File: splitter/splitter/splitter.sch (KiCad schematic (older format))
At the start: 26 parts, among them J1 JACKIN, J2 JACKSEND, J3 JACKRCV, J4 JACKOUT, J5 Barrel_Jack, SW1 SW_HIGHLOW, SW2 SW_POWER, SW3 SW_3PDT_x3, U1 TL074, U2 TLE2426xLP

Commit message: do pcb
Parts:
- removed J5: Barrel_Jack, symbol Connector:Barrel_Jack
- added J5: Jack-DC, Connector_PinSocket_2.54mm:PinSocket_1x02_P2.54mm_Vertical, symbol Connector:Jack-DC
- C1, C2: footprint (none) -> Capacitor_THT:C_Disc_D4.3mm_W1.9mm_P5.00mm
- C3, C4: renamed from C?; footprint (none) -> Capacitor_THT:CP_Radial_D6.3mm_P2.50mm
- D1: renamed from D?; footprint (none) -> LED_THT:LED_D3.0mm
- J1, J2, J3, J4: footprint (none) -> Connector_Audio:Jack_6.35mm_Neutrik_NMJ6HCD2_Horizontal
- R1, R2, R3, R4, R5, R6, R7, R8: footprint (none) -> Resistor_THT:R_Axial_DIN0207_L6.3mm_D2.5mm_P7.62mm_Horizontal
- R9: renamed from R?; footprint (none) -> Resistor_THT:R_Axial_DIN0207_L6.3mm_D2.5mm_P7.62mm_Horizontal
- RV1, RV2: footprint (none) -> Potentiometer_THT:Potentiometer_Alpha_RD902F-40-00D_Dual_Vertical
- SW1: footprint (none) -> Button_Switch_THT:MTS-200_DPDT_6T
- SW2: renamed from SW3; value SW_3PDT_x3 -> SW_POWER; footprint (none) -> Connector_PinSocket_2.54mm:PinSocket_3x03_P2.54mm_Vertical
- SW2: footprint (none) -> Connector_PinSocket_2.54mm:PinSocket_3x03_P2.54mm_Vertical
- U1: footprint (none) -> Package_DIP:DIP-14_W7.62mm
- U2: footprint (none) -> Package_TO_SOT_THT:TO-92_Inline
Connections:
- net GND: now also U2.1 (OUT); no longer U2.2 (COMMON)
- net HIGH: now also U1.1, U1.2 (-); no longer U1.6 (-), U1.7
- net IN: now also U1.5 (+); no longer U1.3 (+)
- net at C2.1, R2.2: now also U1.3 (+); no longer U1.5 (+)
- net at SW2.2 (B): now also J5.1
- net VCC renamed +9V
- net VDD renamed GNDD
- net GNDD: now also U2.2 (COMMON), J5.2; no longer U2.1 (OUT)
- new net: C1.2, U1.6 (-), U1.7
- no-connect marks 2 -> 3
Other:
- note added: "Ground case to GNDD"
- note removed: "Ground case to VDD"
- moved on the sheet: U1A, U1B

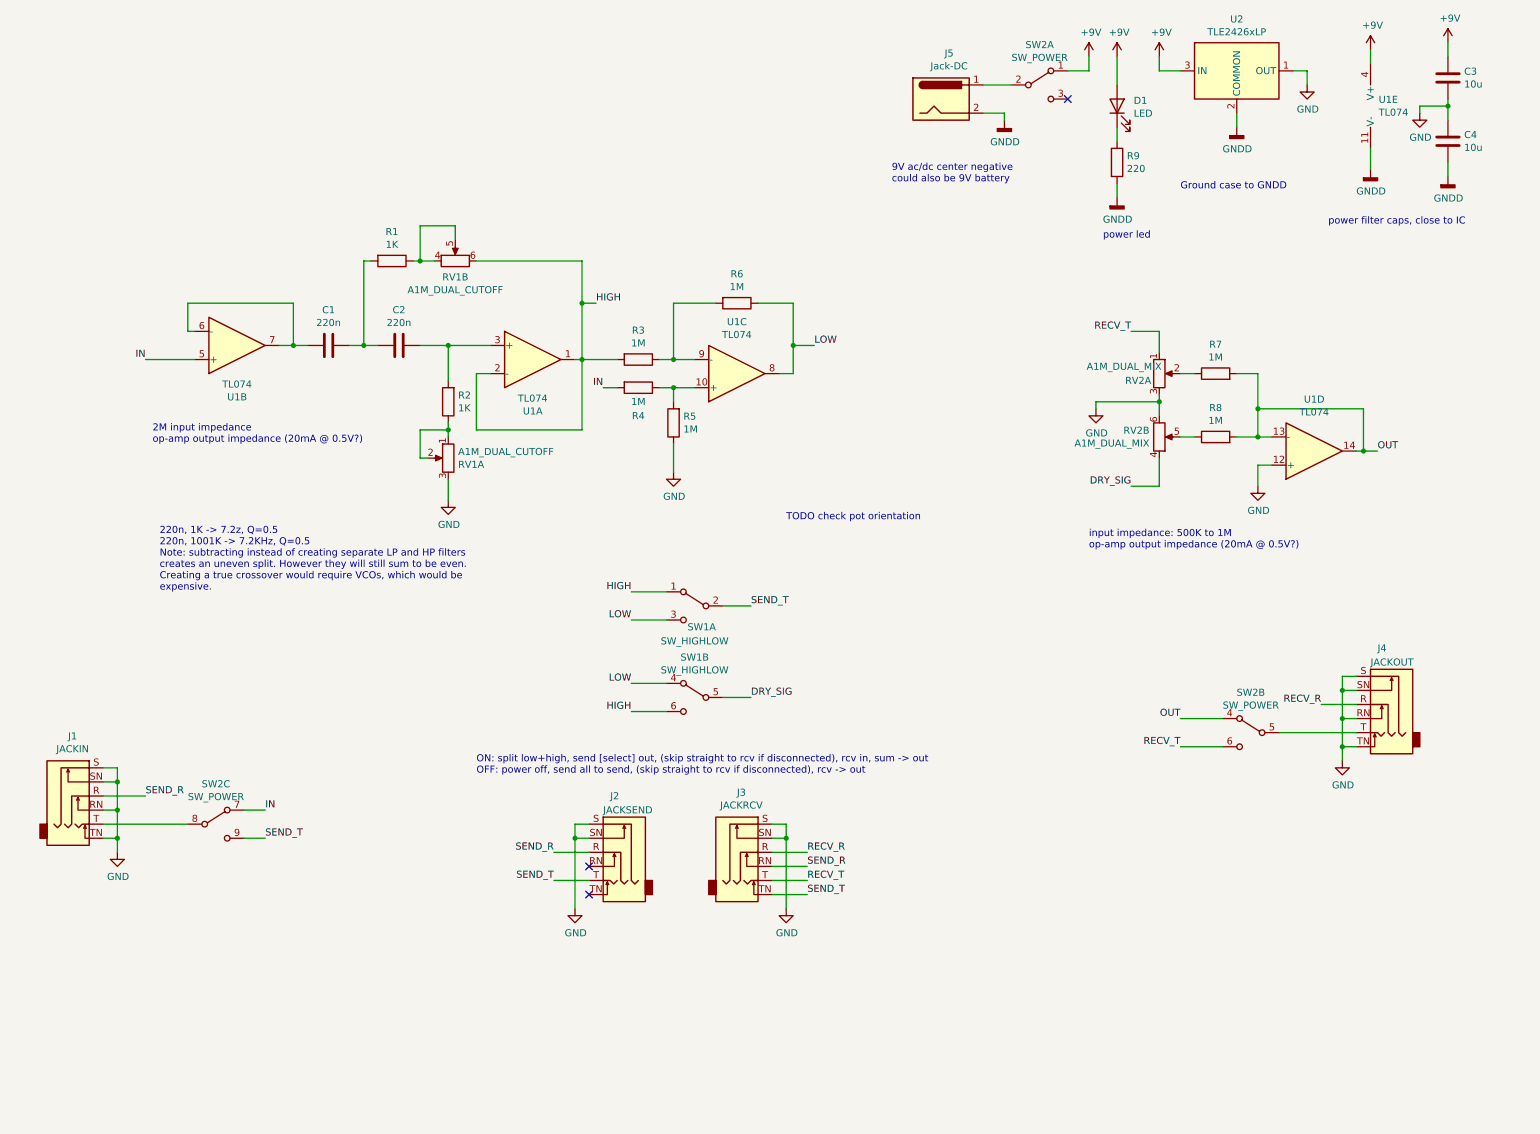
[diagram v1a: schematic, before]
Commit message: rework switches to allow low/high/all send and bypass
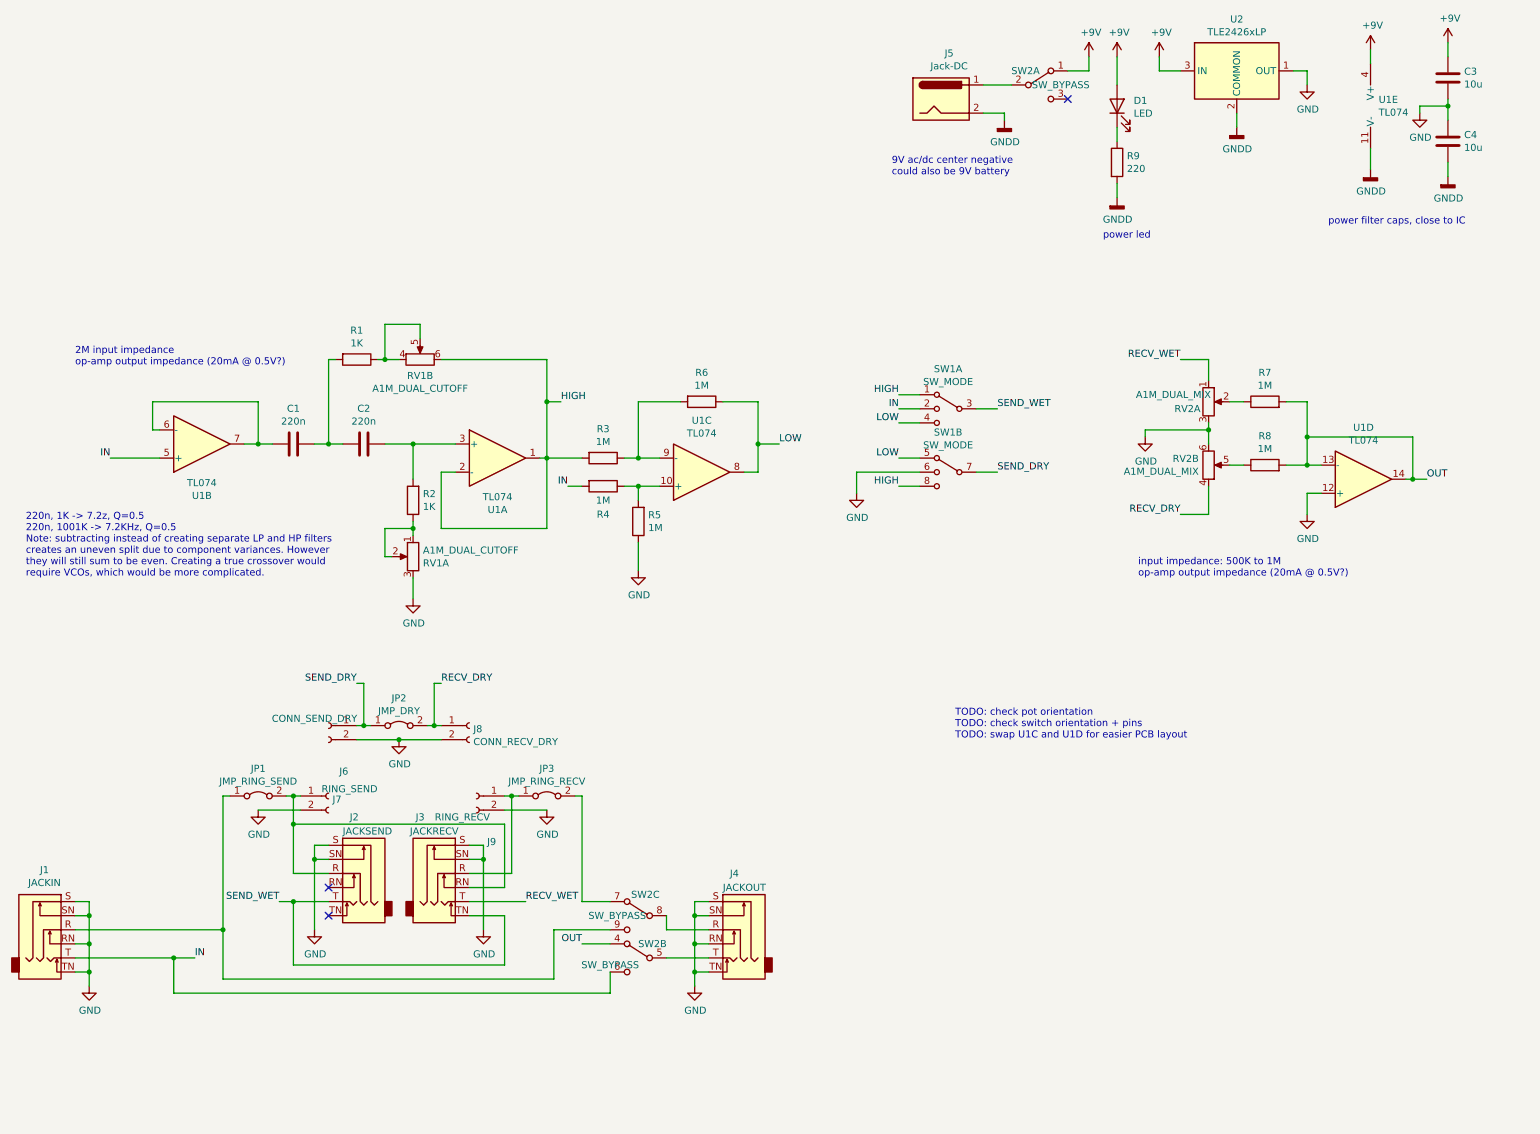
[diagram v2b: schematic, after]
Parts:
- removed SW1: SW_HIGHLOW, Button_Switch_THT:MTS-200_DPDT_6T, symbol Switch:SW_DPDT_x2
- added J6: CONN_SEND_DRY, Connector_PinSocket_2.54mm:PinSocket_1x02_P2.54mm_Vertical, symbol Connector:Conn_01x02_Female
- added J7: RING_SEND, Connector_PinSocket_2.54mm:PinSocket_1x02_P2.54mm_Vertical, symbol Connector:Conn_01x02_Female
- added J8: CONN_RECV_DRY, Connector_PinSocket_2.54mm:PinSocket_1x02_P2.54mm_Vertical, symbol Connector:Conn_01x02_Female
- added J9: RING_RECV, Connector_PinSocket_2.54mm:PinSocket_1x02_P2.54mm_Vertical, symbol Connector:Conn_01x02_Female
- added JP1: JMP_RING_SEND, Jumper:SolderJumper-2_P1.3mm_Open_RoundedPad1.0x1.5mm, symbol Jumper:Jumper_2_Bridged
- added JP2: JMP_DRY, Jumper:SolderJumper-2_P1.3mm_Open_RoundedPad1.0x1.5mm, symbol Jumper:Jumper_2_Bridged
- added JP3: JMP_RING_RECV, Jumper:SolderJumper-2_P1.3mm_Open_RoundedPad1.0x1.5mm, symbol Jumper:Jumper_2_Bridged
- added SW1: SW_MODE, Button_Switch_THT:SW_EG2301_DP3T, symbol Switch:SW_DP3T
- J3: value JACKRCV -> JACKRECV
- SW2: value SW_POWER -> SW_BYPASS
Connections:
- net GND: now also J6.2 (Pin_2), J7.2 (Pin_2), J8.2 (Pin_2), J9.2 (Pin_2), SW1.6
- net HIGH: now also SW1.1, SW1.8
- net IN: now also J1.T, SW2.6 (C), SW1.2; no longer SW2.7 (A)
- net LOW: now also SW1.4, SW1.5
- net at SW2.8 (B): now also J4.R; no longer J1.T
- net DRY_SIG renamed RECV_DRY
- net RECV_DRY: now also J8.1 (Pin_1), JP2.2 (B)
- net RECV_R: no longer names the net of J3.R
- net RECV_R: now also J9.1 (Pin_1), JP3.1 (A); no longer J4.R
- net RECV_T renamed RECV_WET
- net RECV_WET: no longer SW2.6 (C)
- net SEND_R: no longer names the net of J2.R, J3.RN
- net SEND_R: now also J7.1 (Pin_1), JP1.2 (B); no longer J1.R
- net SEND_T renamed SEND_WET
- net SEND_WET: now also SW1.3; no longer SW2.9 (C)
- new net: JP3.2 (B), SW2.7 (A)
- new net: J1.R, JP1.1 (A), SW2.9 (C)
- new net SEND_DRY: J6.1 (Pin_1), JP2.1 (A), SW1.7
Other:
- note added: "220n, 1K -> 7.2z, Q=0.5\n220n, 1001K -> 7.2KHz, Q=0.5\nNote: subtracting instead of creating separate LP and HP filters\ncreates an uneven split due to component variances. However\nthey will still sum to be even. Creating a true crossover would\nrequire VCOs, which would be more complicated."
- note added: "TODO: check pot orientation\nTODO: check switch orientation + pins\nTODO: swap U1C and U1D for easier PCB layout"
- note removed: "220n, 1K -> 7.2z, Q=0.5\n220n, 1001K -> 7.2KHz, Q=0.5\nNote: subtracting instead of creating separate LP and HP filters\ncreates an uneven split. However they will still sum to be even.\nCreating a true crossover would require VCOs, which would be\nexpensive."
- note removed: "Ground case to GNDD"
- note removed: "ON: split low+high, send [select] out, (skip straight to rcv if disconnected), rcv in, sum -> out\nOFF: power off, send all to send, (skip straight to rcv if disconnected), rcv -> out"
- note removed: "TODO check pot orientation"
- moved on the sheet: C1, C2, J1, J2, J3, J4, R1, R2, R3, R4, R5, R6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

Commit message: fix some bugs
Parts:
- added R10: 1M, Resistor_THT:R_Axial_DIN0207_L6.3mm_D2.5mm_P7.62mm_Horizontal, symbol Device:R
- C1, C2: value 220n -> 22n
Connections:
- net GND: now also RV2.1, U1.10 (+); no longer RV2.3, U1.12 (+)
- net LOW: now also U1.14; no longer U1.8
- net OUT: now also U1.8, R10.2; no longer R7.2, R8.2, U1.13 (-), U1.14
- net RECV_DRY: now also RV2.3; no longer RV2.4
- net RECV_WET: now also RV2.4; no longer RV2.1
- net at R4.1, R5.2: now also U1.12 (+); no longer U1.10 (+)
- net at R3.1, R6.2: now also U1.13 (-); no longer U1.9 (-)
- net at R8.1: now also RV2.2; no longer RV2.5
- net at R7.1: now also RV2.5; no longer RV2.2
- new net: R10.1, R7.2, R8.2, U1.9 (-)
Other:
- note added: "22n, 1K -> 7.2z, Q=0.5\n22n, 1001K -> 7.2KHz, Q=0.5\nNote: subtracting instead of creating separate LP and HP\nfilters creates an uneven split as opposed to summing LR\nfilters. Creating a true crossover would require VCOs,\nwhich would be more complicated."
- note added: "TODO: check pot orientation\nTODO: check switch orientation + pins\nTODO: verify mixer on bb\nTODO: verify switching on bb"
- note removed: "220n, 1K -> 7.2z, Q=0.5\n220n, 1001K -> 7.2KHz, Q=0.5\nNote: subtracting instead of creating separate LP and HP filters\ncreates an uneven split due to component variances. However\nthey will still sum to be even. Creating a true crossover would\nrequire VCOs, which would be more complicated."
- note removed: "TODO: check pot orientation\nTODO: check switch orientation + pins\nTODO: swap U1C and U1D for easier PCB layout"
- moved on the sheet: RV2A, RV2B, U1C, U1D
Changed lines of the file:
@@
 P 2700 3600
 F 0 "C1" V 2448 3600 50  0000 C CNN
-F 1 "220n" V 2539 3600 50  0000 C CNN
+F 1 "22n" V 2539 3600 50  0000 C CNN
 F 2 "Capacitor_THT:C_Disc_D4.3mm_W1.9mm_P5.00mm" H 2738 3450 50  0001 C CNN
 F 3 "~" H 2700 3600 50  0001 C CNN
@@
 P 3200 3600
 F 0 "C2" V 2948 3600 50  0000 C CNN
-F 1 "220n" V 3039 3600 50  0000 C CNN
+F 1 "22n" V 3039 3600 50  0000 C CNN
 F 2 "Capacitor_THT:C_Disc_D4.3mm_W1.9mm_P5.00mm" H 3238 3450 50  0001 C CNN
 F 3 "~" H 3200 3600 50  0001 C CNN
@@
 $EndComp
 Text Notes 800  4550 0    50   ~ 0
-220n, 1K -> 7.2z, Q=0.5\n220n, 1001K -> 7.2KHz, Q=0.5\nNote: subtracting instead of creating separate LP and HP filters\ncreates an uneven split due to component variances. However\nthey will still sum to be even. Creating a true crossover would\nrequire VCOs, which would be more complicated.
+22n, 1K -> 7.2z, Q=0.5\n22n, 1001K -> 7.2KHz, Q=0.5\nNote: subtracting instead of creating separate LP and HP\nfilters creates an uneven split as opposed to summing LR\nfilters. Creating a true crossover would require VCOs,\nwhich would be more complicated.
 $Comp
 L Amplifier_Operational:TL074 U1
@@
 $EndComp
 Text Notes 7400 5700 0    50   ~ 0
-TODO: check pot orientation\nTODO: check switch orientation + pins\nTODO: swap U1C and U1D for easier PCB layout
+TODO: check pot orientation\nTODO: check switch orientation + pins\nTODO: verify mixer on bb\nTODO: verify switching on bb
 $Comp
 L power:GND #PWR02
@@
 L Amplifier_Operational:TL074 U1
 U 3 1 62D6659B
-P 5600 3800
-F 0 "U1" H 5600 3433 50  0000 C CNN
-F 1 "TL074" H 5600 3524 50  0000 C CNN
-F 2 "Package_DIP:DIP-14_W7.62mm" H 5550 3900 50  0001 C CNN
-F 3 "http://www.ti.com/lit/ds/symlink/tl071.pdf" H 5650 4000 50  0001 C CNN
-	3    5600 3800
+P 10300 3850
+F 0 "U1" H 10300 3483 50  0000 C CNN
+F 1 "TL074" H 10300 3574 50  0000 C CNN
+F 2 "Package_DIP:DIP-14_W7.62mm" H 10250 3950 50  0001 C CNN
+F 3 "http://www.ti.com/lit/ds/symlink/tl071.pdf" H 10350 4050 50  0001 C CNN
+	3    10300 3850
 	1    0    0    1
 $EndComp
@@
 L Amplifier_Operational:TL074 U1
 U 4 1 62D7837B
-P 10300 3850
-F 0 "U1" H 10300 3483 50  0000 C CNN
-F 1 "TL074" H 10300 3574 50  0000 C CNN
-F 2 "Package_DIP:DIP-14_W7.62mm" H 10250 3950 50  0001 C CNN
-F 3 "http://www.ti.com/lit/ds/symlink/tl071.pdf" H 10350 4050 50  0001 C CNN
-	4    10300 3850
+P 5600 3800
+F 0 "U1" H 5700 4050 50  0000 C CNN
+F 1 "TL074" H 5700 3950 50  0000 C CNN
+F 2 "Package_DIP:DIP-14_W7.62mm" H 5550 3900 50  0001 C CNN
+F 3 "http://www.ti.com/lit/ds/symlink/tl071.pdf" H 5650 4000 50  0001 C CNN
+	4    5600 3800
 	1    0    0    1
 $EndComp
@@
 Connection ~ 9900 3750
 Wire Wire Line
-	9900 3750 10000 3750
+	9900 3750 9950 3750
 $Comp
 L Device:R_POT_Dual_Separate RV2
 U 2 1 62D7EC04
+P 9200 3300
+F 0 "RV2" H 9130 3254 50  0000 R CNN
+F 1 "A1M_DUAL_MIX" H 9130 3345 50  0000 R CNN
+F 2 "Potentiometer_THT:Potentiometer_Alpha_RD902F-40-00D_Dual_Vertical" H 9200 3300 50  0001 C CNN
+F 3 "~" H 9200 3300 50  0001 C CNN
+	2    9200 3300
+	1    0    0    -1
+$EndComp
+$Comp
+L Device:R_POT_Dual_Separate RV2
+U 1 1 62D7FACD
 P 9200 3750
-F 0 "RV2" H 9130 3704 50  0000 R CNN
-F 1 "A1M_DUAL_MIX" H 9130 3795 50  0000 R CNN
+F 0 "RV2" H 9050 3700 50  0000 C CNN
+F 1 "A1M_DUAL_MIX" H 8950 3800 50  0000 C CNN
 F 2 "Potentiometer_THT:Potentiometer_Alpha_RD902F-40-00D_Dual_Vertical" H 9200 3750 50  0001 C CNN
 F 3 "~" H 9200 3750 50  0001 C CNN
-	2    9200 3750
-	1    0    0    1
-$EndComp
-$Comp
-L Device:R_POT_Dual_Separate RV2
-U 1 1 62D7FACD
-P 9200 3300
-F 0 "RV2" H 9050 3250 50  0000 C CNN
-F 1 "A1M_DUAL_MIX" H 8950 3350 50  0000 C CNN
-F 2 "Potentiometer_THT:Potentiometer_Alpha_RD902F-40-00D_Dual_Vertical" H 9200 3300 50  0001 C CNN
-F 3 "~" H 9200 3300 50  0001 C CNN
-	1    9200 3300
+	1    9200 3750
 	1    0    0    -1
 $EndComp
 Wire Wire Line
 	9750 3300 9900 3300
-Wire Wire Line
-	9900 3300 9900 3550
 Wire Wire Line
 	9450 3750 9350 3750
@@
 	9900 3950 10000 3950
 Wire Wire Line
-	9900 3550 10650 3550
-Wire Wire Line
 	10650 3550 10650 3850
 Wire Wire Line
 	10650 3850 10600 3850
-Connection ~ 9900 3550
-Wire Wire Line
-	9900 3550 9900 3750
 $Comp
 L Switch:SW_3PDT_x3 SW2
@@
 Wire Wire Line
 	2700 6300 2700 6650
+Wire Wire Line
+	9900 3300 9900 3750
+$Comp
+L Device:R R10
+U 1 1 640FC6F5
+P 10400 3550
+F 0 "R10" V 10607 3550 50  0000 C CNN
+F 1 "1M" V 10516 3550 50  0000 C CNN
+F 2 "Resistor_THT:R_Axial_DIN0207_L6.3mm_D2.5mm_P7.62mm_Horizontal" V 10330 3550 50  0001 C CNN
+F 3 "~" H 10400 3550 50  0001 C CNN
+	1    10400 3550
+	0    -1   -1   0
+$EndComp
+Wire Wire Line
+	10550 3550 10650 3550
+Wire Wire Line
+	10250 3550 9950 3550
+Wire Wire Line
+	9950 3550 9950 3750
+Connection ~ 9950 3750
+Wire Wire Line
+	9950 3750 10000 3750
 $EndSCHEMATC
